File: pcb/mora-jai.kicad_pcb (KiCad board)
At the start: 2 copper layers, 150 x 150 mm, 77 parts, among them IC1 TPS61023DRLR, J1 Conn_01x02, J2 Conn_01x04, J3 Conn_01x02, J4 Conn_01x01, J5 Conn_01x03, J6 Conn_01x02, SW1 SW_Push, SW10 SW_Push, SW11 SW_Push, SW12 SW_Push, SW13 SW_Push, SW14 SW_Push, SW15 SW_Push, SW16 SW_Push, SW2 SW_Push, SW3 SW_Push, SW4 SW_Push, SW5 SW_Push, SW6 SW_Push, SW7 SW_Push, SW8 SW_Push, SW9 SW_Push, U1 CD74HC4067M, U2 MCP73833-AMI-UN, U3 XIAO-ESP32-S3-SMD

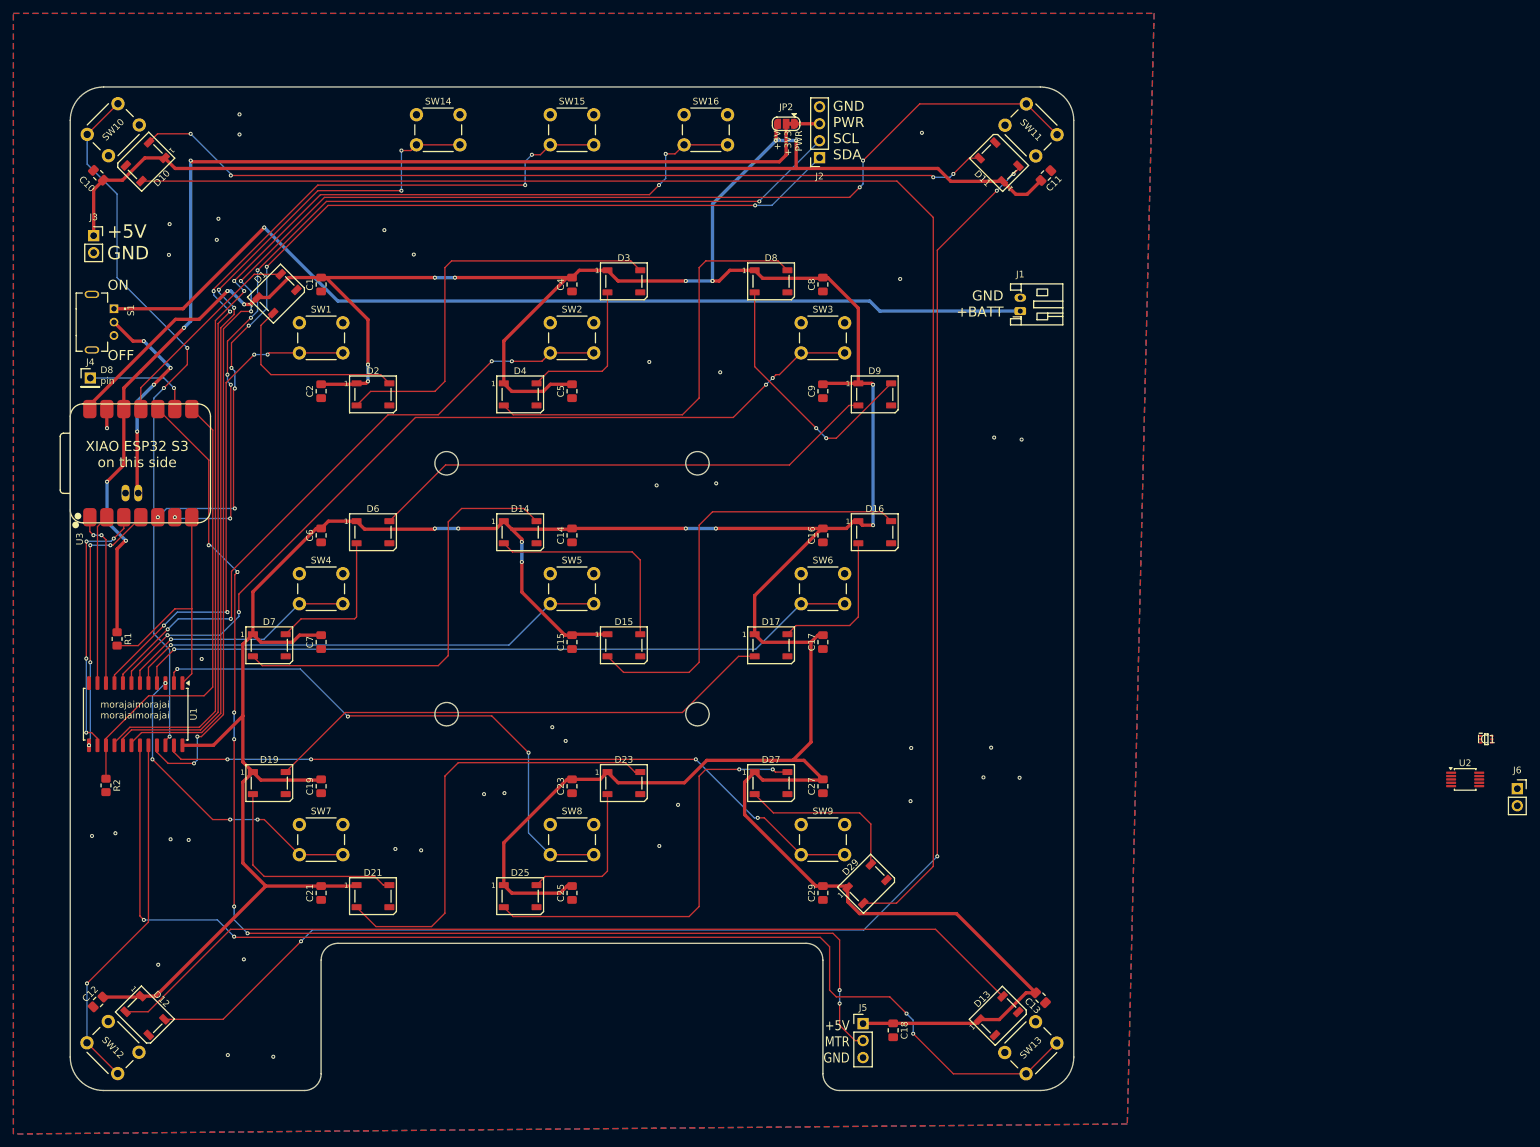
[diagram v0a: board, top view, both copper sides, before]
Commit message: placing power components
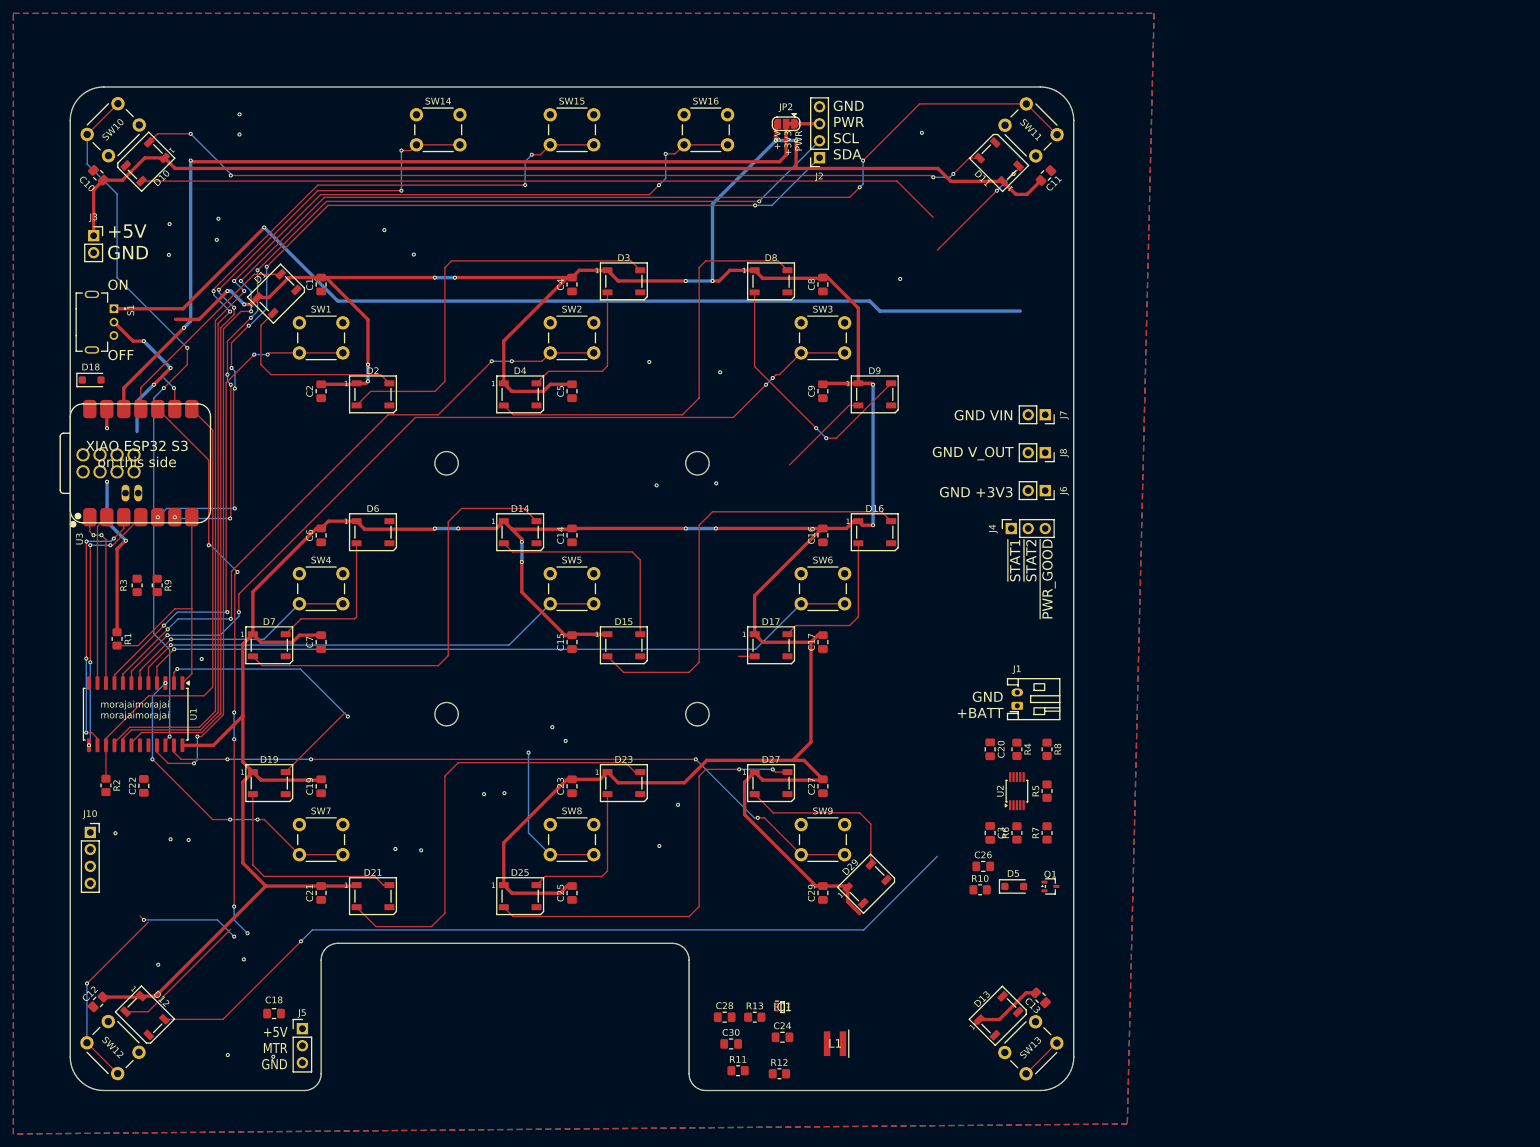
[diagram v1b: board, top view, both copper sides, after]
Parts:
- added C20: 1 uF, Capacitor_SMD:C_0805_2012Metric_Pad1.18x1.45mm_HandSolder, F.Cu at (163.5, 122.0)
- added C22: 1 uF, Capacitor_SMD:C_0805_2012Metric_Pad1.18x1.45mm_HandSolder, F.Cu at (37.0, 127.5)
- added C24: 22 uF, Capacitor_SMD:C_0805_2012Metric_Pad1.18x1.45mm_HandSolder, F.Cu at (132.5, 165.0)
- added C26: 1 uF, Capacitor_SMD:C_0805_2012Metric_Pad1.18x1.45mm_HandSolder, F.Cu at (162.5, 139.5)
- added C28: 22 uF, Capacitor_SMD:C_0805_2012Metric_Pad1.18x1.45mm_HandSolder, F.Cu at (123.8, 162.0)
- added C3: 1 uF, Capacitor_SMD:C_0805_2012Metric_Pad1.18x1.45mm_HandSolder, F.Cu at (163.5, 134.5)
- added C30: 22 uF, Capacitor_SMD:C_0805_2012Metric_Pad1.18x1.45mm_HandSolder, F.Cu at (124.8, 166.0)
- added D18: D_Schottky, Diode_SMD:D_SOD-123F, F.Cu at (29.2, 66.8)
- added D5: D_Schottky, Diode_SMD:D_SOD-123F, F.Cu at (167.1, 142.5)
- added J10: Conn_01x04, Connector_PinSocket_2.54mm:PinSocket_1x04_P2.54mm_Vertical, F.Cu at (29.0, 134.4)
- added J7: Conn_01x02, Connector_PinSocket_2.54mm:PinSocket_1x02_P2.54mm_Vertical, F.Cu at (171.7, 72.0)
- added J8: Conn_01x02, Connector_PinSocket_2.54mm:PinSocket_1x02_P2.54mm_Vertical, F.Cu at (171.7, 77.7)
- added L1: 1 uH, Mora_Jai_Parts:74438356010, F.Cu at (140.3, 166.0)
- added Q1: Q_PMOS_DGS, Package_TO_SOT_SMD:SOT-323_SC-70, F.Cu at (172.5, 142.5)
- added R10: 100kΩ, Resistor_SMD:R_0805_2012Metric_Pad1.20x1.40mm_HandSolder, F.Cu at (162.0, 143.0)
- added R11: 732kΩ, Resistor_SMD:R_0805_2012Metric_Pad1.20x1.40mm_HandSolder, F.Cu at (125.8, 170.0)
- added R12: 100kΩ, Resistor_SMD:R_0805_2012Metric_Pad1.20x1.40mm_HandSolder, F.Cu at (132.0, 170.5)
- added R13: 100kΩ, Resistor_SMD:R_0805_2012Metric_Pad1.20x1.40mm_HandSolder, F.Cu at (128.3, 162.0)
- added R3: 2.2kΩ, Resistor_SMD:R_0805_2012Metric_Pad1.20x1.40mm_HandSolder, F.Cu at (36.0, 97.5)
- added R4: 10kΩ, Resistor_SMD:R_0805_2012Metric_Pad1.20x1.40mm_HandSolder, F.Cu at (167.5, 122.0)
- added R5: 1kΩ, Resistor_SMD:R_0805_2012Metric_Pad1.20x1.40mm_HandSolder, F.Cu at (172.0, 128.2)
- added R6: 100kΩ, Resistor_SMD:R_0805_2012Metric_Pad1.20x1.40mm_HandSolder, F.Cu at (167.5, 134.5)
- added R7: 100kΩ, Resistor_SMD:R_0805_2012Metric_Pad1.20x1.40mm_HandSolder, F.Cu at (172.0, 134.5)
- added R8: 100kΩ, Resistor_SMD:R_0805_2012Metric_Pad1.20x1.40mm_HandSolder, F.Cu at (172.0, 122.0)
- added R9: 10kΩ, Resistor_SMD:R_0805_2012Metric_Pad1.20x1.40mm_HandSolder, F.Cu at (39.0, 97.5)
- J4: value Conn_01x01 -> Conn_01x03; footprint Connector_PinHeader_2.54mm:PinHeader_1x01_P2.54mm_Vertical -> Connector_PinSocket_2.54mm:PinSocket_1x03_P2.54mm_Vertical
- moved J4 139.5 mm to (166.7, 89.0), turned to 90 degrees
- moved IC1 112.5 mm to (132.5, 160.5)
- moved C18 92.6 mm to (56.5, 161.5), turned to 180 degrees
- moved J5 83.8 mm to (60.7, 163.8)
- moved J6 83.5 mm to (171.7, 83.3), turned to -90 degrees
- moved U2 67.0 mm to (167.5, 128.2), turned to 90 degrees
- moved J1 59.0 mm to (167.6, 115.5)
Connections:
- IC1 pad 1: unconnected-(IC1-FB-Pad1) -> Net-(IC1-FB)
- IC1 pad 2: unconnected-(IC1-EN-Pad2) -> Net-(IC1-EN)
- IC1 pad 3: unconnected-(IC1-VIN-Pad3) -> /Power/VIN
- IC1 pad 4: unconnected-(IC1-GND-Pad4) -> GND
- IC1 pad 5: unconnected-(IC1-SW-Pad5) -> Net-(IC1-SW)
- IC1 pad 6: unconnected-(IC1-VOUT-Pad6) -> V_OUT
- J1 pad 1: unconnected-(J1-Pin_1-Pad1) -> +BATT
- J4 pad 1: D8_PIN -> ~{STAT1}
- S1 pad 1: unconnected-(S1-Pad1) -> +5V
- S1 pad 2: unconnected-(S1-Pad2) -> V_OUT
- U3 pad 14: +5V -> Net-(D18-K)
- U3 pad 15: +BATT -> unconnected-(U3-BAT-Pad15)
- U3 pad 16: GND -> unconnected-(U3-GND-Pad16)
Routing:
- net /SW_12: track 179.2 -> 22.0 mm, vias 4 -> 2
- net (no net): track 213.7 -> 68.0 mm, vias 1 -> 0
- net Net-(D12-DOUT): track 140.3 -> 20.8 mm
- net Net-(D10-DIN): track 230.4 -> 120.6 mm
- net MTR_CTRL: track 190.6 -> 84.5 mm, vias 8 -> 6
- net Net-(D11-DOUT): track 233.9 -> 143.3 mm, vias 4 -> 3
- net +5V: track 888.7 -> 967.6 mm, vias 18 -> 19
- net Net-(D6-DIN): track 77.3 -> 14.0 mm
- net Net-(D17-DOUT): track 77.3 -> 15.0 mm
- net +BATT: track 32.1 -> 0.00 mm, vias 4 -> 0
- net /SW_7: track 83.2 -> 54.0 mm
- net /SW_11: track 54.8 -> 28.4 mm
- net V_OUT: track 0.00 -> 22.9 mm, vias 0 -> 3
- net D8_PIN: track 16.3 -> 0.00 mm, vias 1 -> 0
- net +3V3: track 171.6 -> 159.7 mm
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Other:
- outline, holes or cut-outs redrawn
- board text added: "GND +3V3"
- board text added: "GND VIN"
- board text added: "GND V_OUT"
- board text added: "~{STAT1} ~{STAT2} ~{PWR_GOOD}"
- board text removed: "D8 pin"

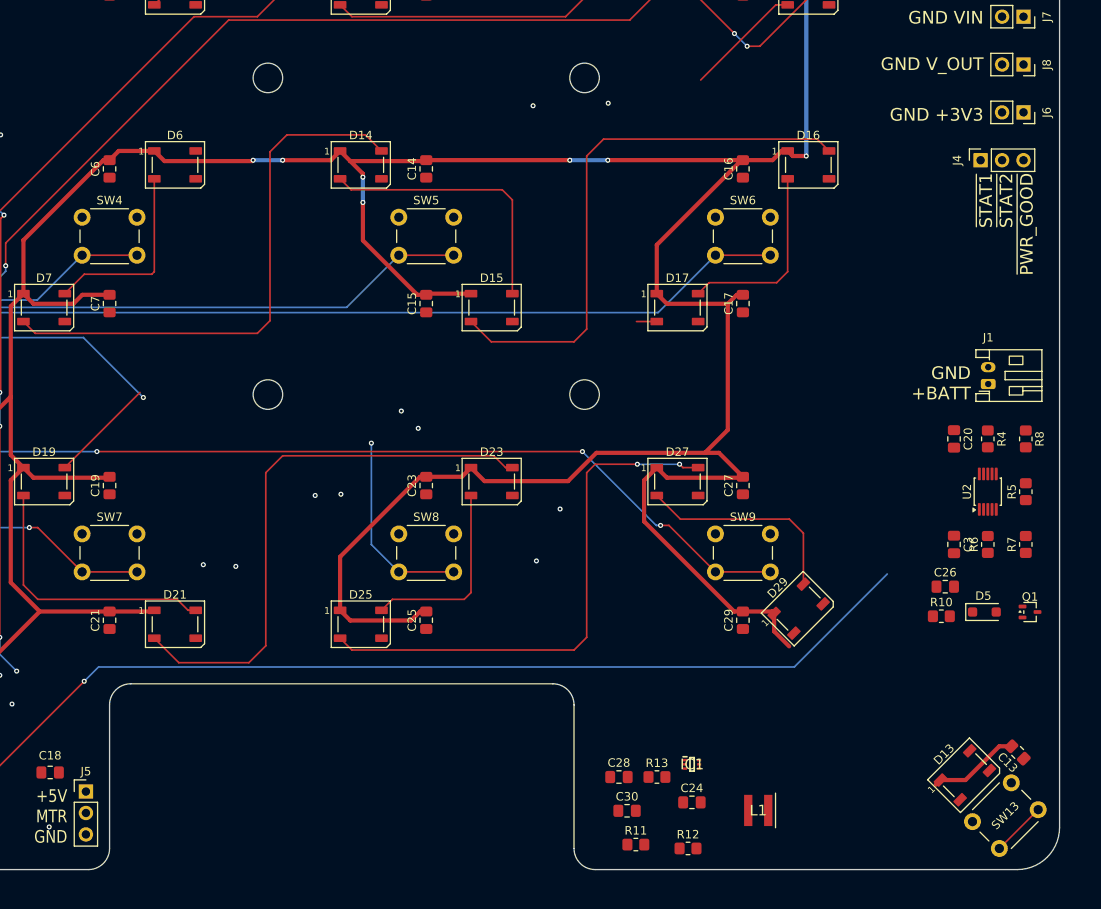
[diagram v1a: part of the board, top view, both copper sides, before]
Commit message: power components all placed, added test pads for all MCU pins
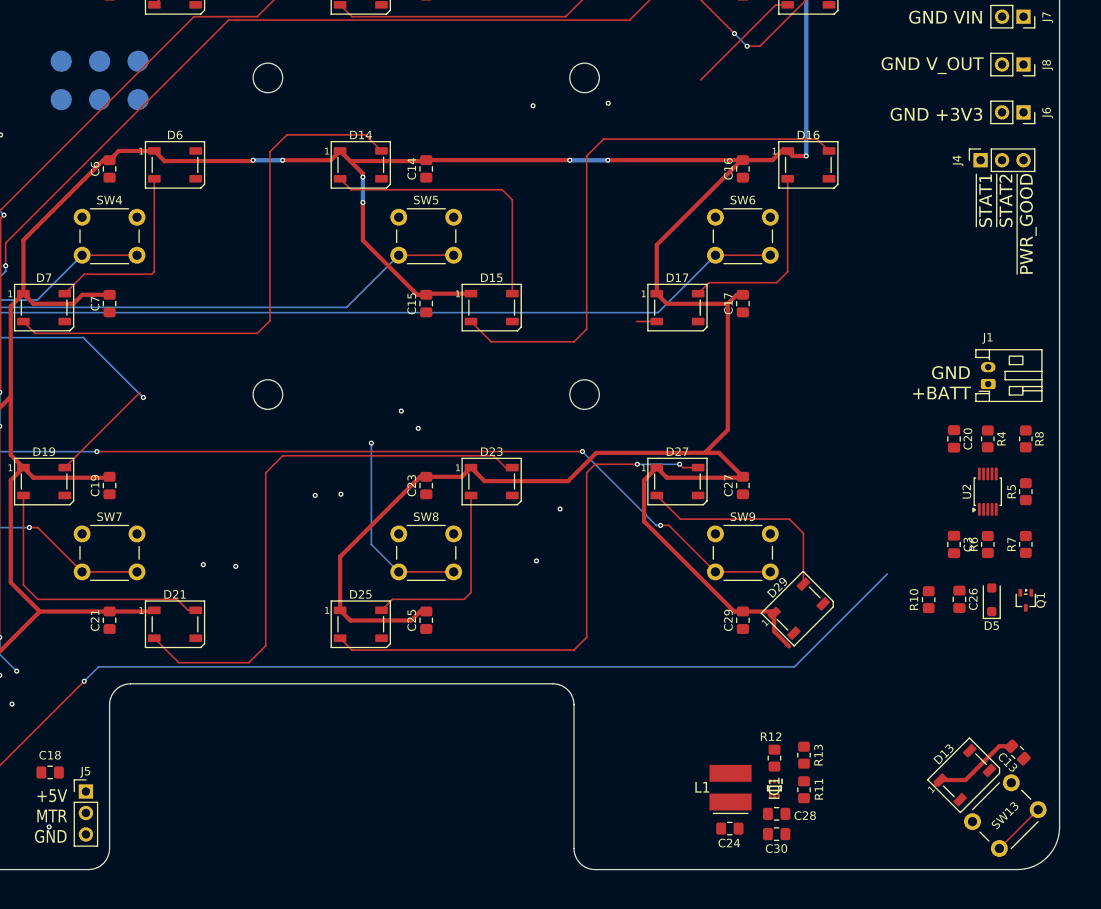
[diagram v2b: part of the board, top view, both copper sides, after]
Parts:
- added TP1: TestPoint, TestPoint:TestPoint_Pad_D2.5mm, B.Cu at (66.9, 77.3)
- added TP2: TestPoint, TestPoint:TestPoint_Pad_D2.5mm, B.Cu at (66.9, 81.8)
- added TP3: TestPoint, TestPoint:TestPoint_Pad_D2.5mm, B.Cu at (62.3, 77.3)
- added TP4: TestPoint, TestPoint:TestPoint_Pad_D2.5mm, B.Cu at (62.3, 81.8)
- added TP5: TestPoint, TestPoint:TestPoint_Pad_D2.5mm, B.Cu at (57.8, 77.3)
- added TP6: TestPoint, TestPoint:TestPoint_Pad_D2.5mm, B.Cu at (57.8, 81.8)
- moved R11 20.9 mm to (145.7, 163.6), turned to 90 degrees
- moved C28 19.2 mm to (142.5, 166.4), turned to 180 degrees
- moved C30 17.9 mm to (142.5, 168.8), turned to 180 degrees
- moved R13 17.6 mm to (145.7, 159.4), turned to -90 degrees
- moved R12 14.8 mm to (142.2, 159.8), turned to -90 degrees
- moved IC1 10.2 mm to (142.2, 163.4), turned to -90 degrees
- moved C24 5.46 mm to (136.9, 168.2)
- moved L1 4.25 mm to (137.0, 163.3), turned to -90 degrees
- moved R10 2.47 mm to (160.5, 141.0), turned to -90 degrees
- moved C26 2.25 mm to (164.1, 141.0), turned to -90 degrees
- moved D5 1.69 mm to (168.0, 141.1), turned to 90 degrees
- moved Q1 1.47 mm to (172.0, 141.1), turned to -90 degrees
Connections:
- U3 pad 15: unconnected-(U3-BAT-Pad15) -> ESPBAT
- U3 pad 16: unconnected-(U3-GND-Pad16) -> GND
- U3 pad 18: unconnected-(U3-MTDO-Pad18) -> MTDO
- U3 pad 19: unconnected-(U3-CHIP_EN-Pad19) -> CHIP_EN
- U3 pad 22: unconnected-(U3-MTCK-Pad22) -> MTCK
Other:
- board text added: "TODO: - Route fill traces for battery charger & boost circuits"
- board text removed: "TODO: - Add battery charger & boost circuits (see schematic)"
